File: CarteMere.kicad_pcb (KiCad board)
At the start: 2 copper layers, 85 x 96 mm, 41 parts, among them J1 Conn_01x04:LIDAR_Data, J2 Conn_01x02, J3 Conn_01x02, J4 Conn_01x03, J5 Conn_01x03, J6 Conn_01x03, J7 Conn_01x04, J8 Conn_01x04, Q1 2N7000, Q2 Q_PMOS_DGS, Q3 PMBT2222A_215, U1 TEENSY3.6, U10 R-78C5.0-1.0, U11 TMC2130, U12 TMC2130, U2 R-78C5.0-1.0, U3 AMS1117-3.3, U4 I2C_Conn, U5 VL52L0X_simple, U6 VL52L0X_simple, U7 TEENSY3.2, U8 VL52L0X_simple, U9 VL52L0X_simple

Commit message: Mise à jour
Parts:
- added D2: LED, LED_THT:LED_D5.0mm, F.Cu at (56.8, 84.2)
- added D3: LED, LED_THT:LED_D5.0mm, F.Cu at (56.8, 104.2)
- added D4: LED, LED_THT:LED_D5.0mm, F.Cu at (129.8, 67.8)
- added D5: LED, LED_THT:LED_D5.0mm, F.Cu at (129.8, 60.8)
- added R10: R, Resistor_SMD:R_1206_3216Metric_Pad1.42x1.75mm_HandSolder, B.Cu at (124.0, 60.5)
- added R11: R, Resistor_SMD:R_1206_3216Metric_Pad1.42x1.75mm_HandSolder, B.Cu at (124.0, 57.5)
- added R8: R, Resistor_SMD:R_1206_3216Metric_Pad1.42x1.75mm_HandSolder, B.Cu at (58.5, 91.8)
- added R9: R, Resistor_SMD:R_1206_3216Metric_Pad1.42x1.75mm_HandSolder, B.Cu at (58.5, 97.0)
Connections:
- U1 pad 11: Net-(U1-Pad11) -> /LED_S1
- U1 pad 12: Net-(U1-Pad12) -> /LED_S2
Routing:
- net +24V: track 75.4 -> 168.5 mm, vias 0 -> 2
- net +3V3: track 72.6 -> 154.1 mm, vias 2 -> 4
- net GND: track 292.0 -> 366.3 mm, vias 5 -> 11
- net Net-(R11-Pad2): track 0.00 -> 68.1 mm, vias 0 -> 2
- net Net-(R10-Pad2): track 0.00 -> 61.9 mm, vias 0 -> 2
- net Net-(D4-Pad2): track 0.00 -> 7.53 mm
- net Net-(D5-Pad2): track 0.00 -> 4.56 mm
- net +5V: track 137.0 -> 141.6 mm
- net Net-(D2-Pad2): track 0.00 -> 4.20 mm
- net Net-(D3-Pad2): track 0.00 -> 3.95 mm
- net /LED_S1: track 0.00 -> 3.52 mm
- net /LED_S2: track 0.00 -> 3.41 mm
- added copper zone on B.Cu, net +3V3
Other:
- board text added: "+ -"
- board text added: "USB"
- board text added: "USB ->"

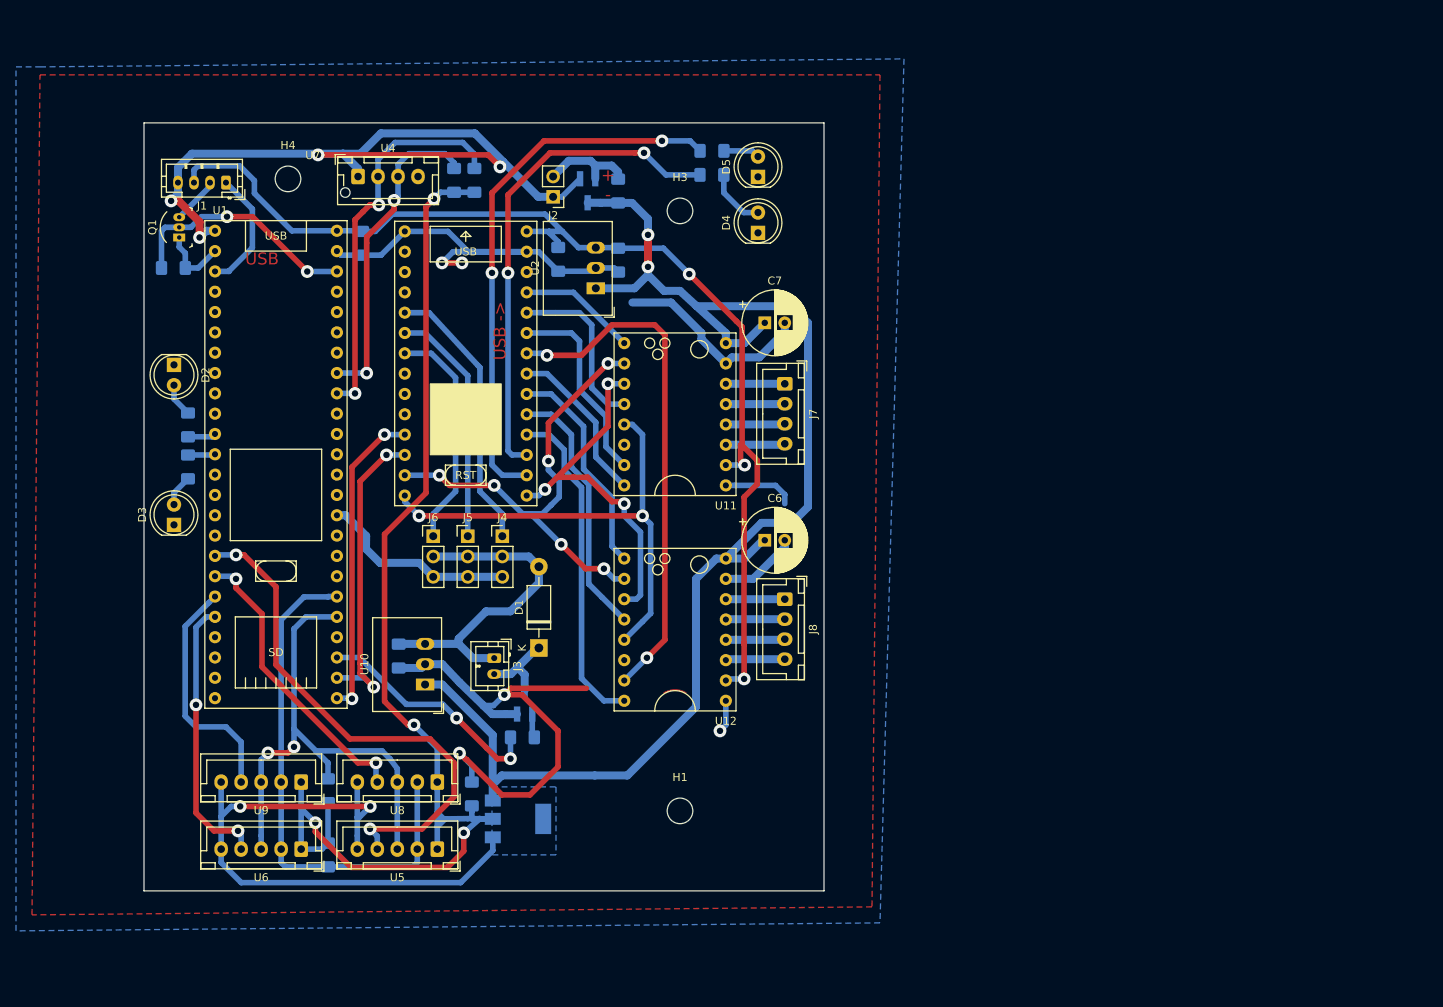
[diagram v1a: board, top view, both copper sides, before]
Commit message: Nettoyage du schéma, ajout de l'UART 4 sur Teensy 3.6 pour debug, renforcement alimentation 5V
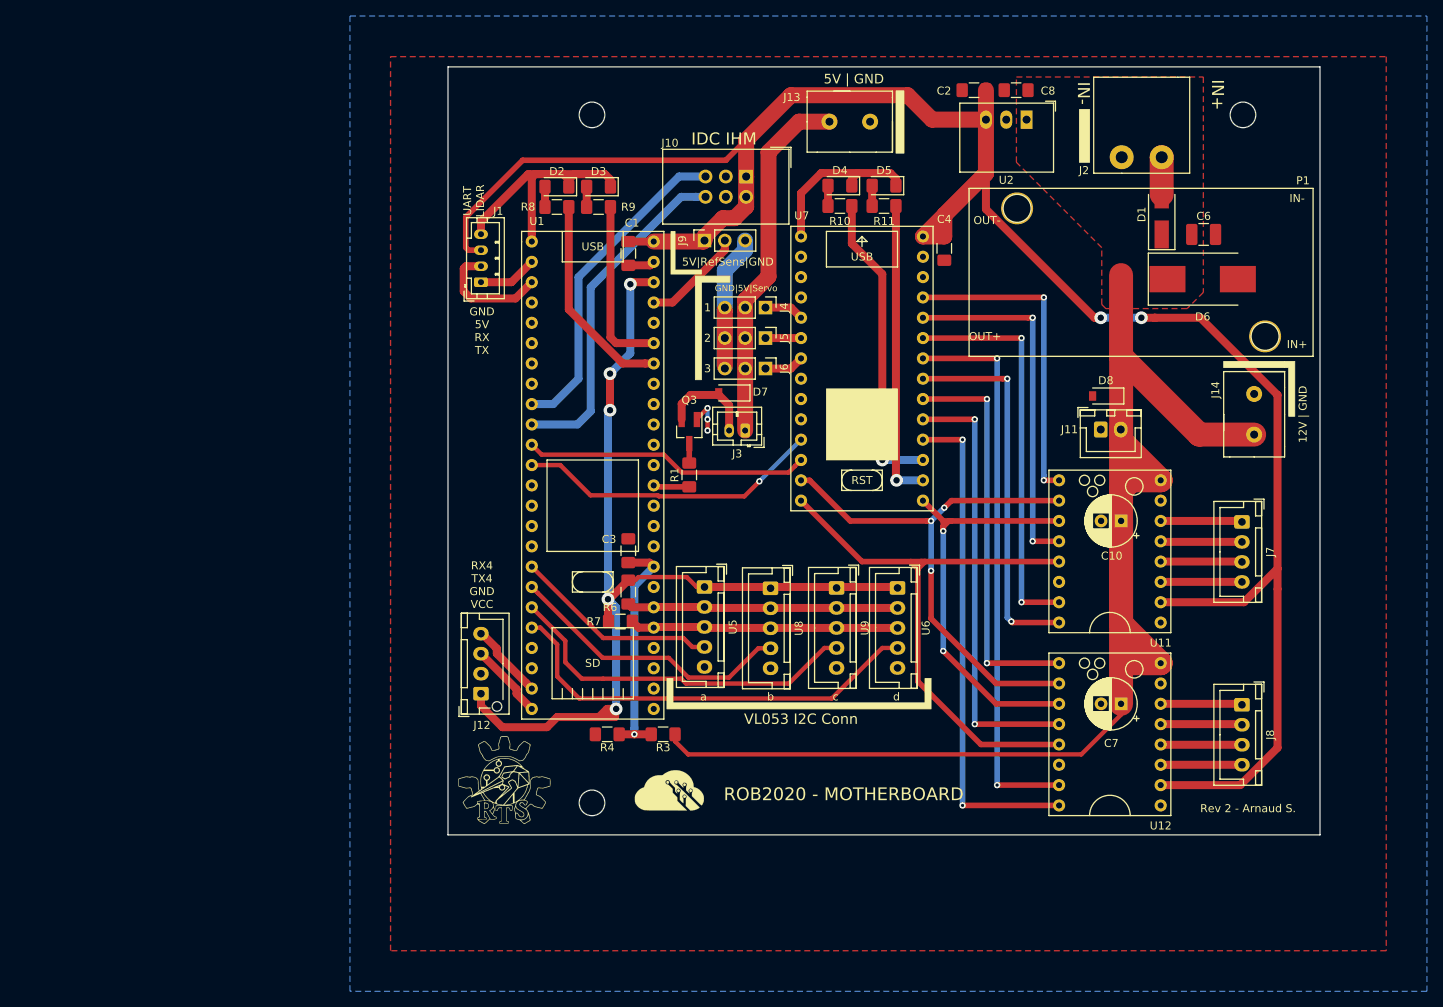
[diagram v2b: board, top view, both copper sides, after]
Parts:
- removed C5: 10uF MLCC, Capacitor_SMD:C_1206_3216Metric_Pad1.42x1.75mm_HandSolder
- removed Q1: 2N7000, digikey-footprints:TO-92-3
- removed Q2: Q_PMOS_DGS, CFR2020_A:SOT-23_DGS_Handsoldering
- removed R2: 10kR_pullup_shifter, Resistor_SMD:R_1206_3216Metric_Pad1.42x1.75mm_HandSolder
- removed R5: R, Resistor_SMD:R_1206_3216Metric_Pad1.42x1.75mm_HandSolder
- removed U10: R-78C5.0-1.0, Converter_DCDC:Converter_DCDC_RECOM_R-78E-0.5_THT
- removed U3: AMS1117-3.3, Package_TO_SOT_SMD:SOT-223-3_TabPin2
- removed U4: I2C_Conn, Connector_JST:JST_XH_B4B-XH-AM_1x04_P2.50mm_Vertical
- added C10: 100uF,25V, Capacitor_THT:CP_Radial_D6.3mm_P2.50mm, F.Cu at (175.1, 103.8)
- added C8: 10 uF 25V MLCC, Capacitor_SMD:C_1206_3216Metric_Pad1.42x1.75mm_HandSolder, F.Cu at (162.0, 49.9)
- added D6: SM30T15AY, Diode_SMD:D_SMC_Handsoldering, F.Cu at (185.3, 73.5)
- added D7: 1N4148, Diode_SMD:D_SOD-123, F.Cu at (126.5, 87.8)
- added D8: 1N4148, Diode_SMD:D_SOD-123, F.Cu at (173.2, 88.1)
- added J10: Conn_02x03, Connector_IDC:IDC-Header_2x03_P2.54mm_Vertical, F.Cu at (128.3, 60.7)
- added J11: Conn_01x02_Fan, Connector_JST:JST_XH_B2B-XH-A_1x02_P2.50mm_Vertical, F.Cu at (172.6, 92.3)
- added J12: Conn_01x04_Male, Connector_JST:JST_XH_B4B-XH-AM_1x04_P2.50mm_Vertical, F.Cu at (95.1, 125.3)
- added J13: Conn_01x02_LM2596_OUT, rex:BatConn, F.Cu at (141.2, 53.8)
- added J14: Conn_01x02_LM2596_IN, rex:BatConn, F.Cu at (191.8, 90.4)
- added J9: Conn_01x03_Male, Connector_PinSocket_2.54mm:PinSocket_1x03_P2.54mm_Vertical, F.Cu at (123.1, 68.7)
- added L1: AISLER_LOGO, Logo:aisler, F.Cu at (118.6, 137.4)
- added L2: RTS_LOGO, Logo:rts, F.Cu at (98.0, 136.1)
- added P1: LM2596Module, CFR2020_A:LM2596 Module, F.Cu at (199.1, 83.2)
- C1: value 10uF_ tant -> 10uF tant 1206; moved to F.Cu
- C2: value 10uF MLCC -> 10uF 16V MLCC; moved to F.Cu
- C3: value 10uF MLCC -> 10uF 9V; moved to F.Cu
- C4, Q3: moved to F.Cu
- C6: value 100uF -> 470 uF, 50V, 1210; footprint Capacitor_THT:CP_Radial_D8.0mm_P2.50mm -> Capacitor_SMD:C_1210_3225Metric_Pad1.42x2.65mm_HandSolder
- C7: value 100uF -> 100uF,25V; footprint Capacitor_THT:CP_Radial_D8.0mm_P2.50mm -> Capacitor_THT:CP_Radial_D6.3mm_P2.50mm
- D1: value DIODE -> D_Schottky; footprint Diode_THT:D_DO-41_SOD81_P10.16mm_Horizontal -> Diode_SMD:D_SMA_Handsoldering
- D2, D3, D4, D5: footprint LED_THT:LED_D5.0mm -> LED_SMD:LED_1206_3216Metric_Pad1.42x1.75mm_HandSolder
- J2: value Conn_01x02 -> Conn_01x02_Male; footprint Connector_PinHeader_2.54mm:PinHeader_1x02_P2.54mm_Vertical -> CFR2020_A:OSTOQ027151
- R1: value 0R_Jumper -> 1.1K, 0.25W, 1206; moved to F.Cu
- R10, R11, R8, R9: value R -> 1kR; moved to F.Cu
- R3: value R -> 30kohm 1206 1/4W; moved to F.Cu
- R4: value R -> 10kohm 1206 1/4W; moved to F.Cu
- R6, R7: value R -> 1k 1206 1/4W; moved to F.Cu
- U1: value TEENSY3.6 -> TEENSY3.5
- moved H4 119.6 mm to (190.4, 53.0)
- moved D1 94.9 mm to (180.2, 65.4)
- moved U6 81.4 mm to (147.2, 112.1), turned to 270 degrees
- moved J2 76.2 mm to (180.2, 58.3)
- moved R3 73.2 mm to (117.9, 130.4), turned to 0 degrees
- moved U9 71.2 mm to (139.6, 112.1), turned to 270 degrees
- moved D3 67.8 mm to (109.8, 62.0), turned to 180 degrees
- moved C6 66.9 mm to (185.5, 67.9)
- moved C7 65.2 mm to (175.1, 126.6), turned to 180 degrees
- moved R9 60.7 mm to (109.8, 64.5), turned to 0 degrees
- moved J7 59.7 mm to (190.2, 103.9)
- moved J8 58.7 mm to (190.2, 126.7)
- moved U2 57.8 mm to (163.3, 53.6), turned to 180 degrees
- moved U11 57.0 mm to (180.1, 116.5)
- moved U12 55.9 mm to (180.1, 139.3)
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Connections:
- net Net-(R10-Pad2) renamed /LED_M1
- net Net-(R11-Pad2) renamed /LED_M2
- C1 pad 1: GND -> +5V
- C1 pad 2: +5V -> GND
- C3 pad 1: +3V3 -> /V_sens
- C6 pad 1: +24V -> +12V
- C7 pad 1: +24V -> +12V
- D1 pad 1: Net-(D1-Pad1) -> +12V
- D1 pad 2: +5VP -> Net-(D1-Pad2)
- J1 pad 2: /RX_LIDAR_5V -> /RX_LIDAR
- J2 pad 1: GND -> Net-(D1-Pad2)
- J2 pad 2: Net-(J2-Pad2) -> GND
- J3 pad 2: Net-(D1-Pad1) -> Net-(D7-Pad2)
- Q3 pad 3: Net-(D1-Pad1) -> Net-(D7-Pad2)
- R1 pad 1: Net-(J2-Pad2) -> /PWM_LIDAR
- R1 pad 2: +24V -> Net-(Q3-Pad1)
- R3 pad 1: /SDA0 -> /V_sens
- R3 pad 2: +3V3 -> +12V
- R4 pad 1: Net-(Q3-Pad1) -> GND
- R4 pad 2: /PWM_LIDAR -> /V_sens
- U1 pad 10: Net-(U1-Pad10) -> /TX3_strat
- U1 pad 11: /LED_S1 -> /RX_Strat
- U1 pad 12: /LED_S2 -> /RX_MOVNT
- U1 pad 2: /RX_LIDAR_3V3 -> /TX_LIDAR
- U1 pad 23: Net-(U1-Pad23) -> /RX4
- U1 pad 24: Net-(U1-Pad24) -> /TX4
- U1 pad 25: /RX_MOVNT -> Net-(U1-Pad25)
- U1 pad 26: /RX_Strat -> Net-(U1-Pad26)
- U1 pad 27: /PWM_LIDAR -> Net-(U1-Pad27)
- U1 pad 3: /TX_LIDAR -> /RX_LIDAR
- U1 pad 32: Net-(U1-Pad32) -> /V_sens
- U1 pad 36: Net-(U1-Pad36) -> /PWM_LIDAR
- U1 pad 40: /SDA0 -> Net-(U1-Pad40)
- U1 pad 41: /SCL0 -> Net-(U1-Pad41)
- U1 pad 42: Net-(U1-Pad42) -> /LED_S1
- U1 pad 43: Net-(U1-Pad43) -> /LED_S2
- U1 pad 45: Net-(U1-Pad45) -> /A0_Reflec_sensor
- U1 pad 46: /3.3V_T36 -> +3V3
- U1 pad 9: Net-(U1-Pad9) -> /RX3_strat
- U11 pad 8: +24V -> +12V
- U12 pad 8: +24V -> +12V
- U2 pad 1: +24V -> +12V
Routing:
- net GND: track 366.3 -> 93.5 mm, vias 11 -> 3
- net +12V: track 0.00 -> 186.1 mm
- net +24V: track 168.5 -> 0.00 mm, vias 2 -> 0
- net +5V: track 141.6 -> 271.9 mm, vias 3 -> 2
- net /SDA0: track 48.8 -> 0.00 mm, vias 2 -> 0
- net /TX3_strat: track 0.00 -> 42.6 mm
- net /RX3_strat: track 0.00 -> 40.9 mm
- net /SCL0: track 40.2 -> 0.00 mm, vias 2 -> 0
- net /XSHUTa: track 65.7 -> 25.7 mm, vias 2 -> 0
- net /SCL1_strat: track 65.9 -> 33.5 mm, vias 2 -> 0
- net /SDA1_strat: track 66.0 -> 33.9 mm
- net +3V3: track 154.1 -> 123.4 mm, vias 4 -> 5
- net /LED_M2: track 68.1 -> 37.6 mm, vias 2 -> 1
- net /3.3V_T36: track 30.1 -> 0.00 mm, vias 2 -> 0
- net /Servo1: track 34.6 -> 4.97 mm
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- added copper zone on F.Cu, net +12V
- removed copper zone on B.Cu, net +3V3
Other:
- board size 85 x 96 mm -> 109 x 96 mm
- board text added: "1"
- board text added: "12V | GND"
- board text added: "2"
- board text added: "3"
- board text added: "5V | GND"
- board text added: "5V|RefSens|GND"
- board text added: "GND 5V RX TX"
- board text added: "GND|5V|Servo"
- board text added: "IDC IHM"
- board text added: "IN+"
- board text added: "IN-"
- board text added: "ROB2020 - MOTHERBOARD"
- board text added: "RX4 TX4 GND VCC"
- board text added: "Rev 2 - Arnaud S."
- board text added: "UART LIDAR"
- board text added: "VL053 I2C Conn"
- board text added: "a"
- board text added: "b"
- board text added: "c"
- board text added: "d"
- board text removed: "+ -"
- board text removed: "USB"
- board text removed: "USB ->"
